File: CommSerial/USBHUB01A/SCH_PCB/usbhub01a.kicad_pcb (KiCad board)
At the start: 4 copper layers, 80.8 x 80.8 mm, 140 parts, among them CON1 PowerIn +5V, J1 OverCurrent, J12 I2C, J13 USB3_A, J14 USB3_B, J15 USB3_A, J16 USB3_A, J17 USB3_A, J18 JUMP_3X2, J2 Test & Misc Signals, M1 HOLE, M2 HOLE, M3 HOLE, M4 HOLE, SW1 SPST, U1 CAT24C04YI-GT3OSCT-ND, U2 TUSB8041IPAPRQ1, U3 TPS7A4533KTTR, U4 TPS74801RGWR, U5 TPS2001CDGN, U6 TPS2001CDGN, U7 TPS2001CDGN, U8 TPS2001CDGN, Y1 24MHz

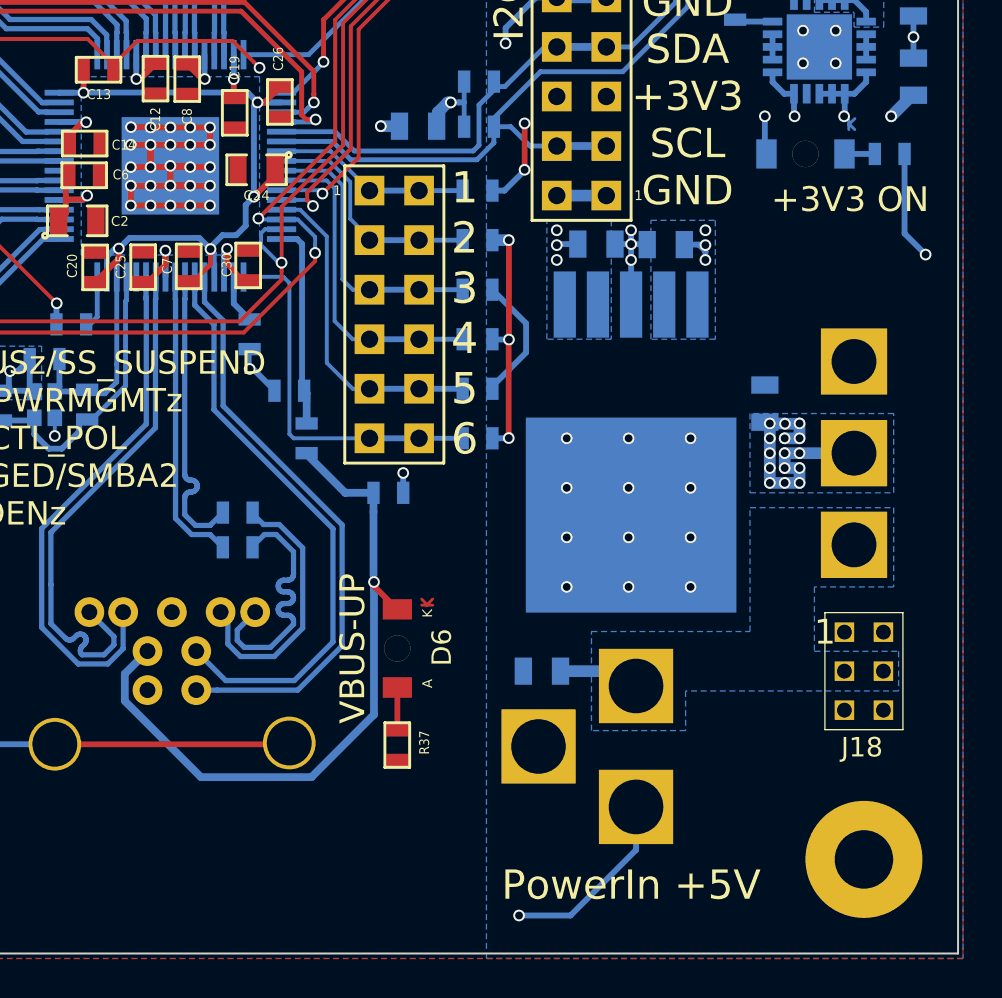
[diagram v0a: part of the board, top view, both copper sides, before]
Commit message: Vyhozený vypínač, přidaný "Distribution Load Switch"
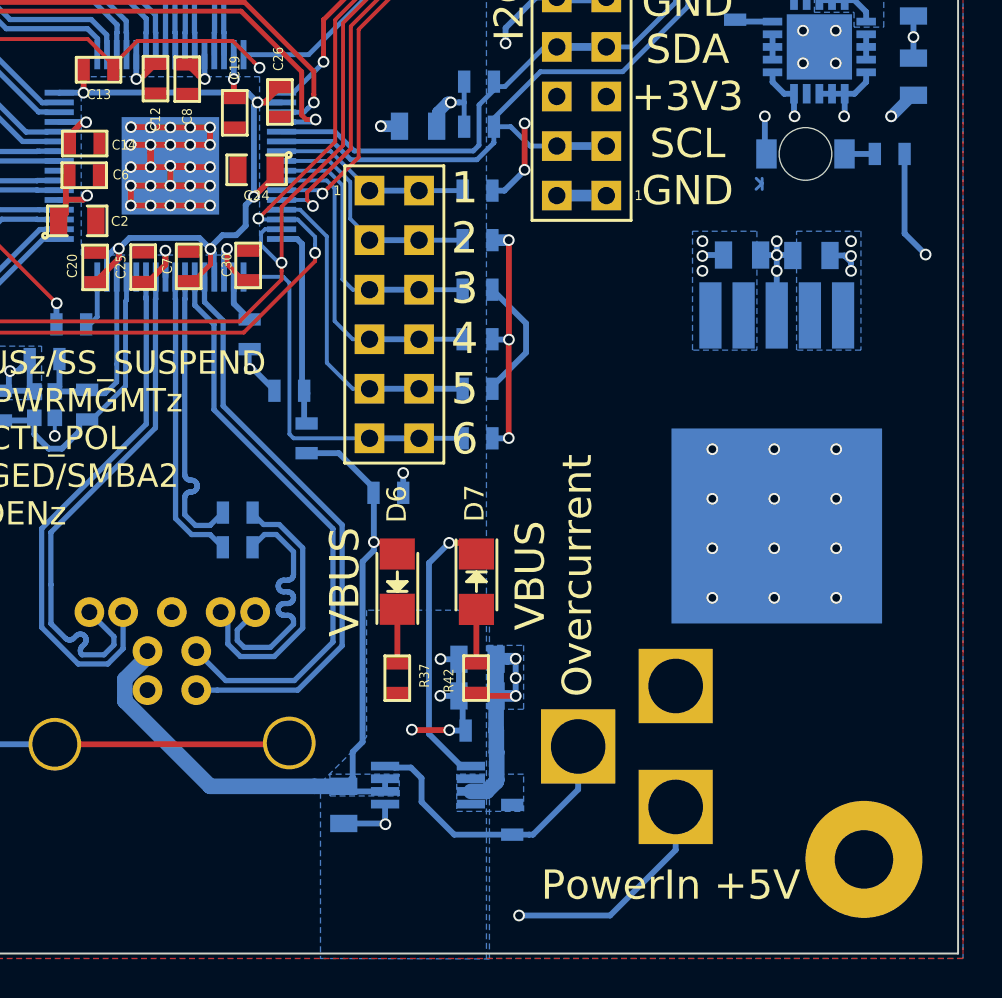
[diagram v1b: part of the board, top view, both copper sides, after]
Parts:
- removed J18: JUMP_3X2, Mlab_Pin_Headers:Straight_2x03
- removed SW1: SPST, Mlab_SW:Prepinaci_3A_SL19121
- added C1: 10uF, Mlab_R:SMD-0805, B.Cu at (163.1, 128.8)
- added C3: 100nF, Mlab_R:SMD-0603, B.Cu at (163.2, 130.6)
- added D7: LED, LEDs:LED_1206, F.Cu at (163.0, 122.9)
- added R41: 10k, Mlab_R:SMD-0603, B.Cu at (164.8, 135.1)
- added R42: 470R, Mlab_R:SMD-0603, F.Cu at (163.0, 127.9)
- added U9: AP22811, Housings_SSOP:MSOP-8_3x3mm_Pitch0.65mm, B.Cu at (160.5, 133.3)
- C35: value 10uF -> 1uF
- D1: value +3V3 ON -> +3V3
- D6: footprint Mlab_D:LED_1206 -> LEDs:LED_1206
- moved C37 19.7 mm to (163.1, 126.9), turned to 180 degrees
- moved C35 12.3 mm to (156.2, 134.4), turned to 270 degrees
- moved C38 7.49 mm to (180.2, 106.2)
- moved C36 7.49 mm to (176.6, 106.2)
- moved U3 7.49 mm to (178.4, 109.3)
- moved D6 3.43 mm to (159.0, 122.9)
- moved R37 3.43 mm to (159.0, 127.9)
- moved CON1 2.03 mm to (173.2, 132.1)
- turned D1 to 180 degrees
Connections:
- C35 pad 1: Net-(C35-Pad1) -> /USB_VBUS_UP
- CON1 pad 1: Net-(C35-Pad1) -> +5V
- CON1 pad 3: GND -> Net-(CON1-Pad3)
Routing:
- net Net-(CON1-Pad3): track 0.00 -> 15.2 mm
- net Net-(D7-Pad1): track 0.00 -> 14.5 mm, vias 0 -> 1
- net GND: track 241.9 -> 255.7 mm, vias 96 -> 101
- net +5V: track 58.2 -> 65.3 mm, vias 30 -> 18
- net Net-(C35-Pad1): track 4.19 -> 0.00 mm
- net Net-(D7-Pad2): track 0.00 -> 2.16 mm
- net +3V3: track 223.3 -> 222.8 mm
- net /USB_VBUS_UP: track 39.8 -> 40.3 mm
- added copper zone on B.Cu, net /USB_VBUS_UP
- removed copper zone on B.Cu, net Net-(C35-Pad1)
- removed copper zone on In1.Cu, net Net-(C35-Pad1)
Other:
- board text added: "VBUS"
- board text added: "VBUS Overcurrent"

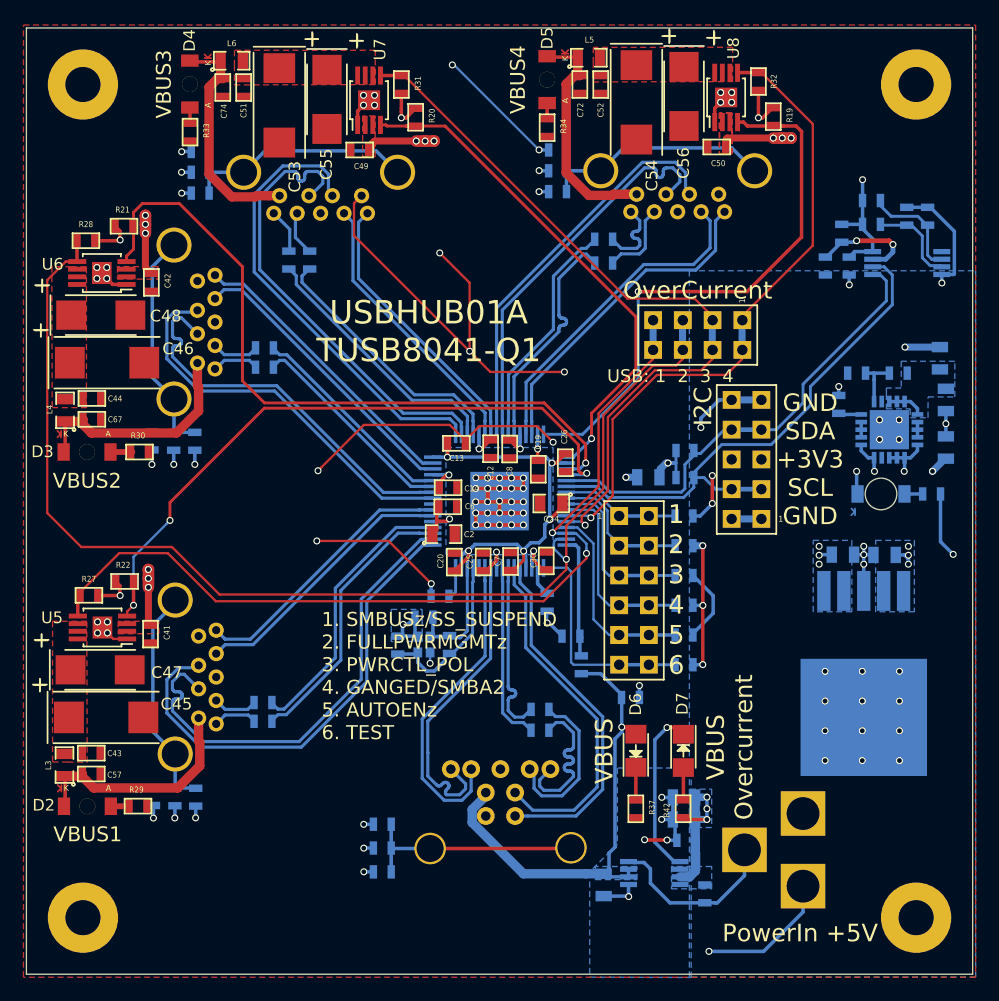
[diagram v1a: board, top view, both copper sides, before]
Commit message: Přidání tantalového kondenzátoru na +5V větev
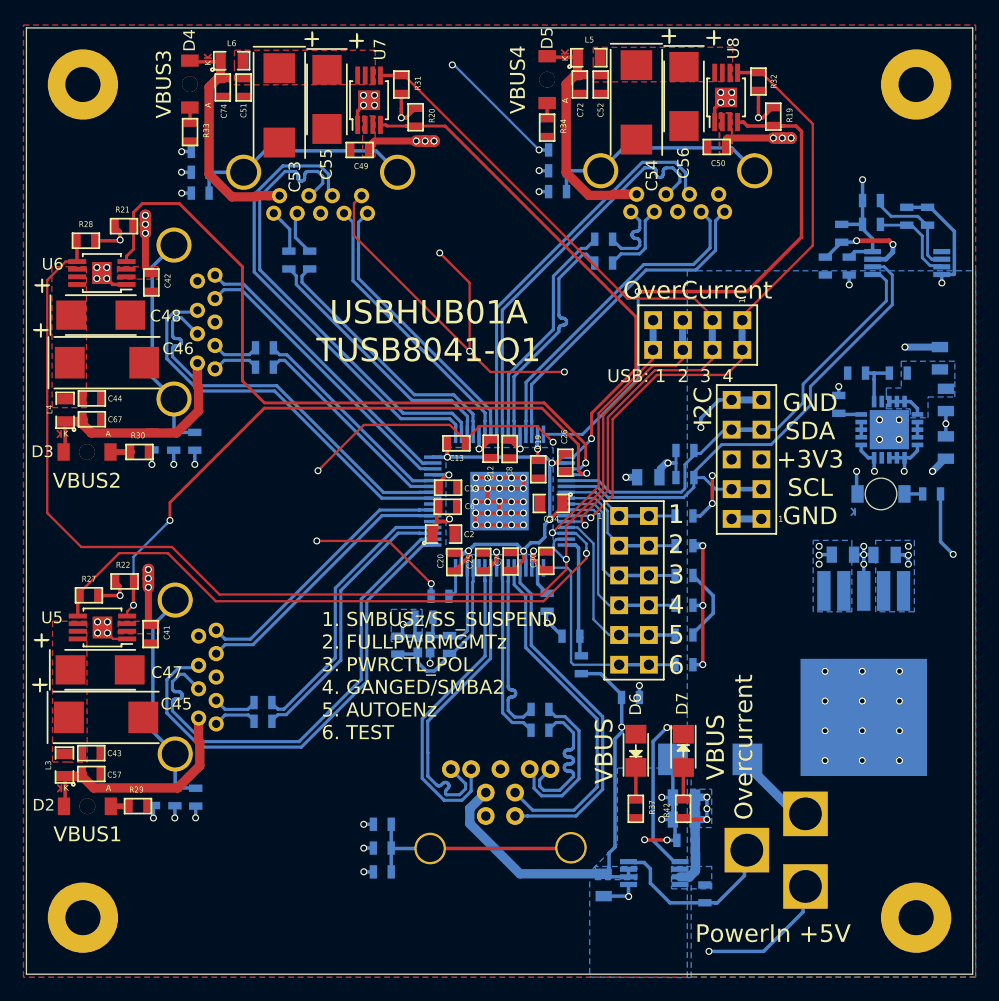
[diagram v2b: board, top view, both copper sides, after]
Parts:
- added C4: 100uF, Mlab_C:TantalC_SizeD_Reflow, B.Cu at (165.3, 123.6)
- moved CON1 0.20 mm to (173.4, 132.1)
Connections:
- U1 pad 1: Net-(U1-Pad1) -> (no net)
- U2 pad 28: Net-(U2-Pad28) -> (no net)
- U2 pad 40: Net-(U2-Pad40) -> (no net)
- U4 pad 17: Net-(U4-Pad17) -> (no net)
- U4 pad 9: Net-(U4-Pad9) -> (no net)
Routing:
- net +5V: track 65.3 -> 71.6 mm
- net GND: track 255.7 -> 258.4 mm
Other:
- net class Default: clearance 0 -> 0.2
- rule trace_clearance: 0 -> 0.2

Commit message: USB-Hub-funkcni finalni verze
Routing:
- net +3V3: track 222.8 -> 225.5 mm
- net GND: track 258.4 -> 259.2 mm
- net /AUTOENZ_HS_SUS: track 16.9 -> 16.3 mm
- net /PWRCTL_POL_TDO: track 14.6 -> 14.1 mm
- net /GANGED_SMBA2_SH_UP: track 16.6 -> 16.1 mm
